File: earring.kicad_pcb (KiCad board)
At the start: 2 copper layers, 39.4 x 41.9 mm, 98 parts, among them J2 USB_C_Receptacle_USB2.0, Q1 NMOS 20V 0.75A 500mΩ@4.5V, Q2 NMOS 20V 0.75A 500mΩ@4.5V, Q3 NMOS 20V 0.75A 500mΩ@4.5V, Q4 NMOS 20V 0.75A 500mΩ@4.5V, U1 Magnetic Switch, U10 USBLC6-2P6, U20 LGS4056H, U3 RP2040, U4 W25Q16JV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

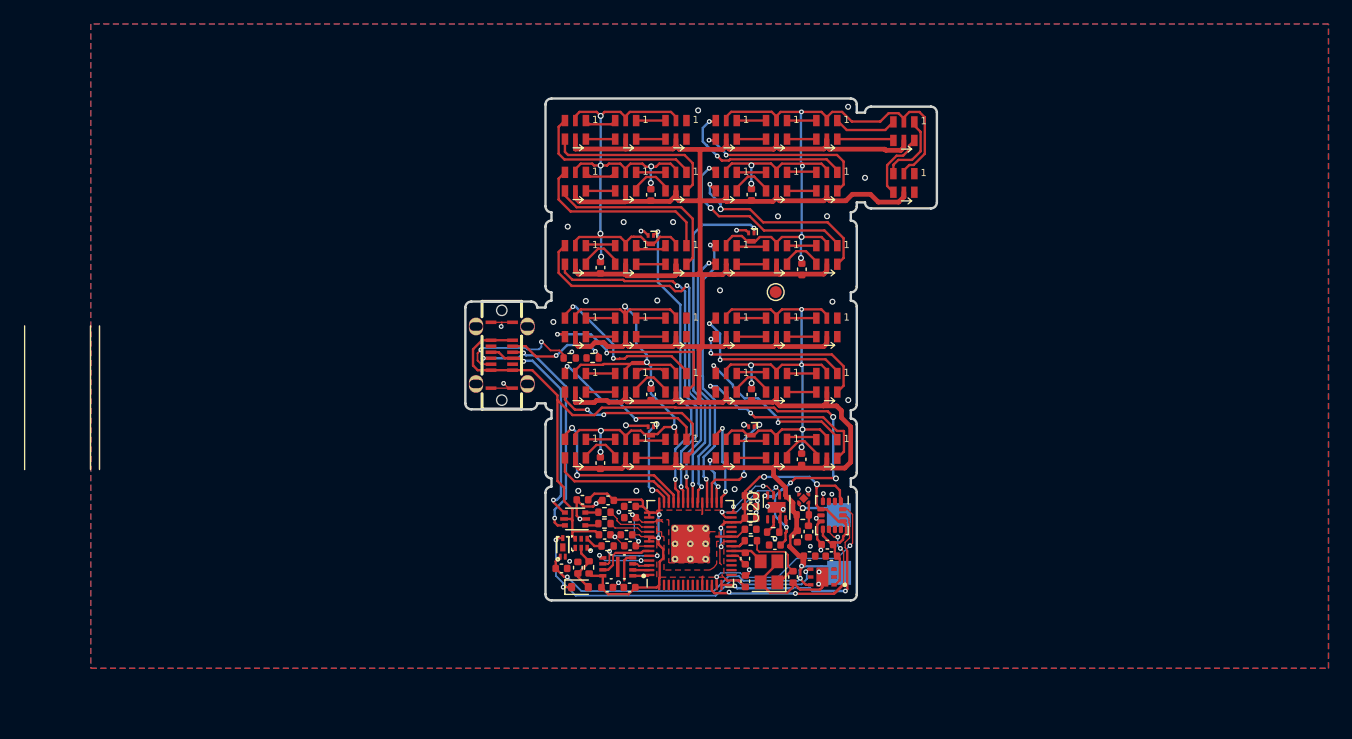
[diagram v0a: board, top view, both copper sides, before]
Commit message: Updated files, nearly complete. Added stiffener layer.
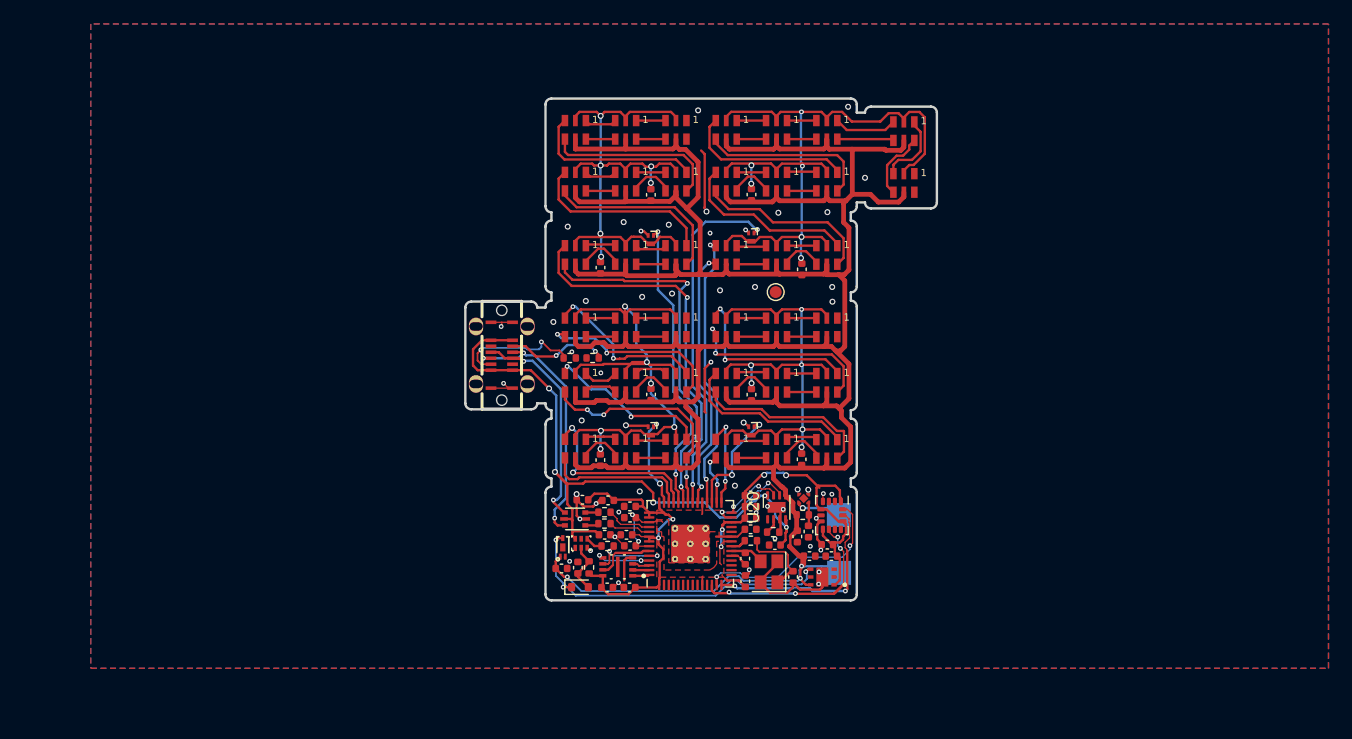
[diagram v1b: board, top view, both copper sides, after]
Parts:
- R10: value ~ -> 20k
- U9: value ~ -> NCP730BMT330TBG
- moved C26 0.25 mm to (154.6, 93.2)
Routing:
- net VBUS: track 71.2 -> 55.6 mm
- net +BATT: track 248.7 -> 264.0 mm
- net GND: track 38.2 -> 47.0 mm, vias 45 -> 51
- net +3V3: track 61.9 -> 64.0 mm
- net Net-(U34-CKL): track 16.9 -> 15.0 mm, vias 2 -> 0
- net Net-(U34-SDI): track 16.6 -> 14.9 mm, vias 2 -> 0
- net /LED_SCK_3: track 30.0 -> 31.1 mm
- net Net-(U27-CKL): track 15.3 -> 14.3 mm, vias 2 -> 0
- net Net-(U19-CKL): track 15.9 -> 14.9 mm, vias 2 -> 0
- net /LED_TX_4: track 14.7 -> 15.7 mm
- net Net-(U16-CKL): track 15.6 -> 16.5 mm
- net /LED_SCK_4: track 11.2 -> 12.1 mm
- net Net-(U27-SDI): track 15.0 -> 14.1 mm, vias 2 -> 0
- net /LED_TX_3: track 33.2 -> 32.4 mm
- net Net-(U15-CKO): track 16.5 -> 15.7 mm
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
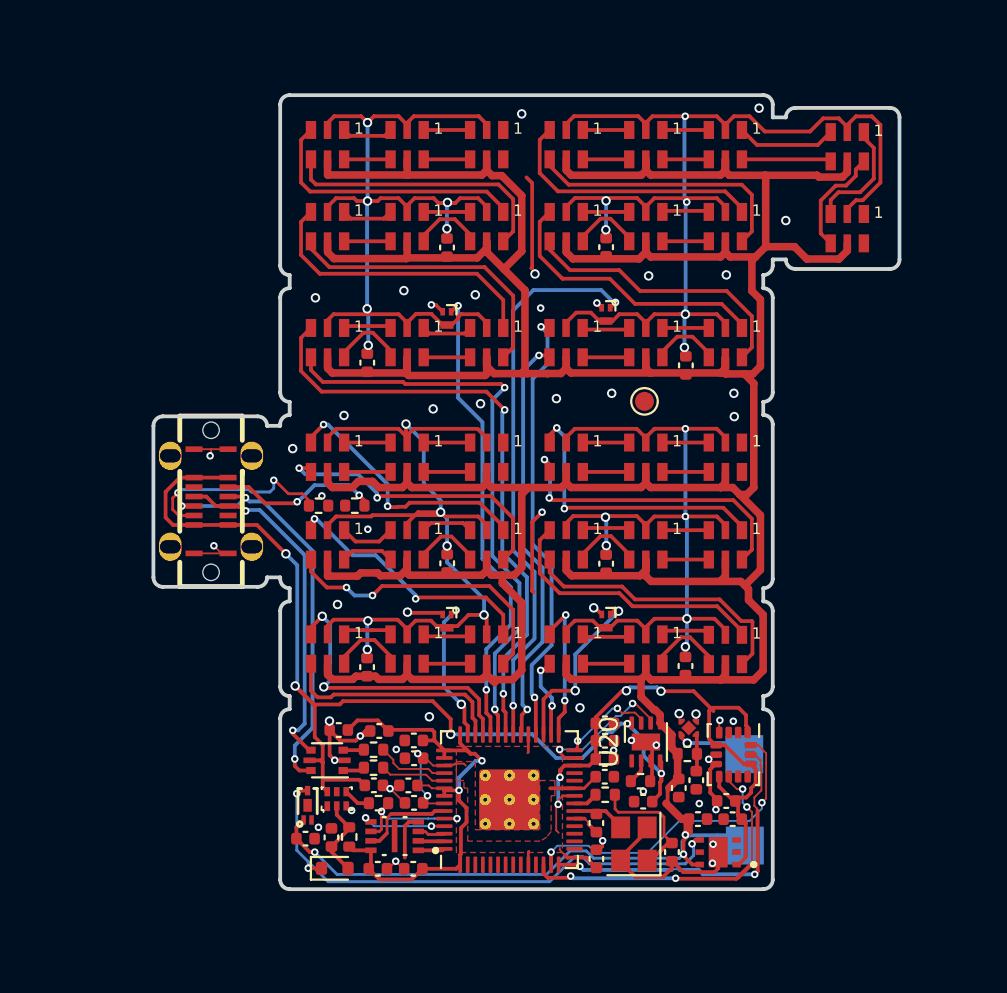
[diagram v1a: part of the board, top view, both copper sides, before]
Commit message: Add light sensor, add more 3d models.
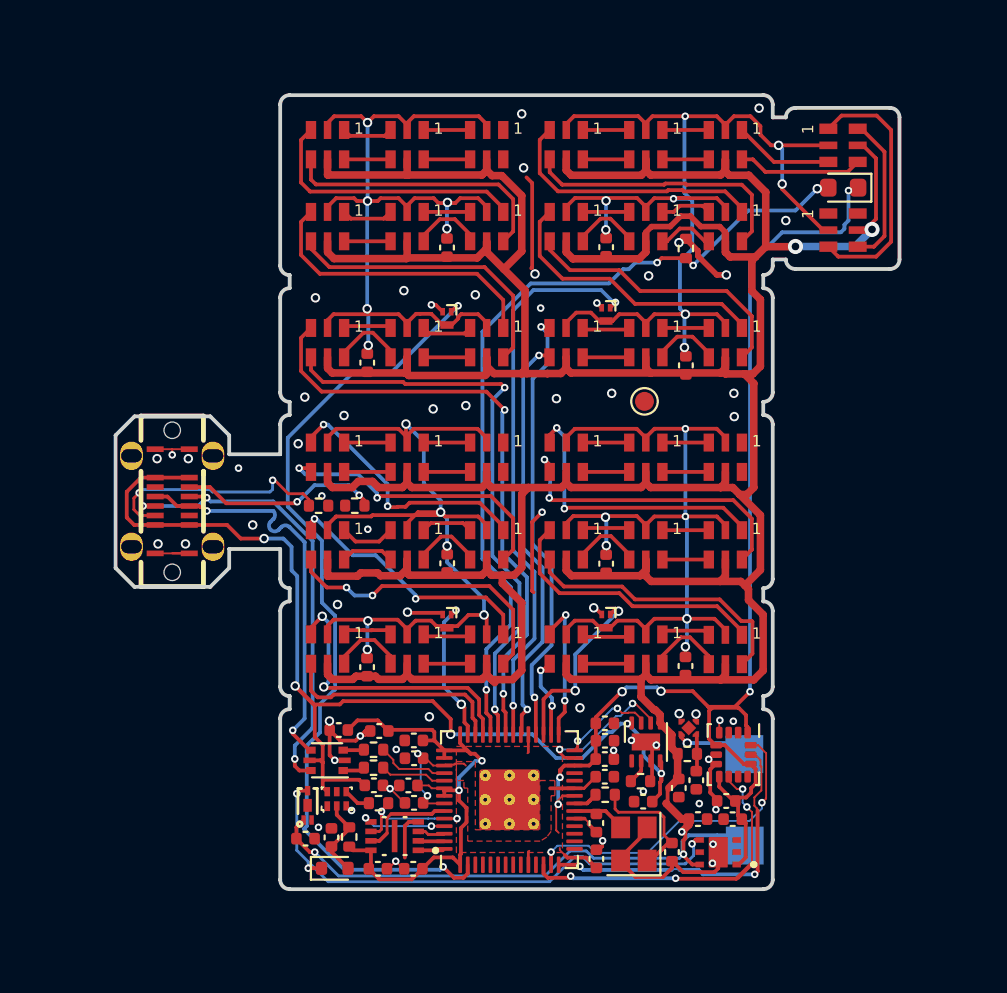
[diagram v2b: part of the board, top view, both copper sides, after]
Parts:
- added Q5: ~, LED_SMD:LED_0603_1608Metric, F.Cu at (179.7, 67.9)
- added R8: WHAT VALUE?, Resistor_SMD:R_0402_1005Metric, F.Cu at (171.4, 71.1)
- U24: value ~ -> SK9822-EC20
- moved J2 2.05 mm to (144.3, 84.5)
- moved U30 0.24 mm to (179.7, 65.7), turned to 90 degrees
- moved U37 0.24 mm to (179.7, 70.1), turned to 90 degrees
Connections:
- U3 pad 2: unconnected-(U3-GPIO0-Pad2) -> /SW_LED_3
- U3 pad 38: /SW_LED_3 -> /LIGHT_SENSE
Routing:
- net /LIGHT_SENSE: track 0.00 -> 44.2 mm, vias 0 -> 4
- net +3V3: track 64.0 -> 97.1 mm, vias 6 -> 8
- net /SW_LED_3: track 24.9 -> 45.1 mm
- net Net-(U30-SDO): track 6.16 -> 13.7 mm
- net /USB_D-: track 18.3 -> 21.6 mm
- net GND: track 47.0 -> 50.0 mm, vias 51 -> 59
- net VBUS: track 55.6 -> 58.1 mm
- net +BATT: track 264.0 -> 266.4 mm, vias 3 -> 5
- net /USB_D+: track 22.5 -> 24.9 mm
- net Net-(U30-CKO): track 5.80 -> 8.02 mm
- net Net-(J2-CC1): track 10.5 -> 12.6 mm
- net Net-(J2-CC2): track 8.55 -> 10.6 mm
- net Net-(U29-CKO): track 4.73 -> 6.60 mm
- net /LED_2_GND: track 61.5 -> 59.8 mm, vias 6 -> 8
- net Net-(U35-CKO): track 2.45 -> 3.01 mm
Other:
- board size 39.4 x 41.9 mm -> 41.4 x 41.9 mm

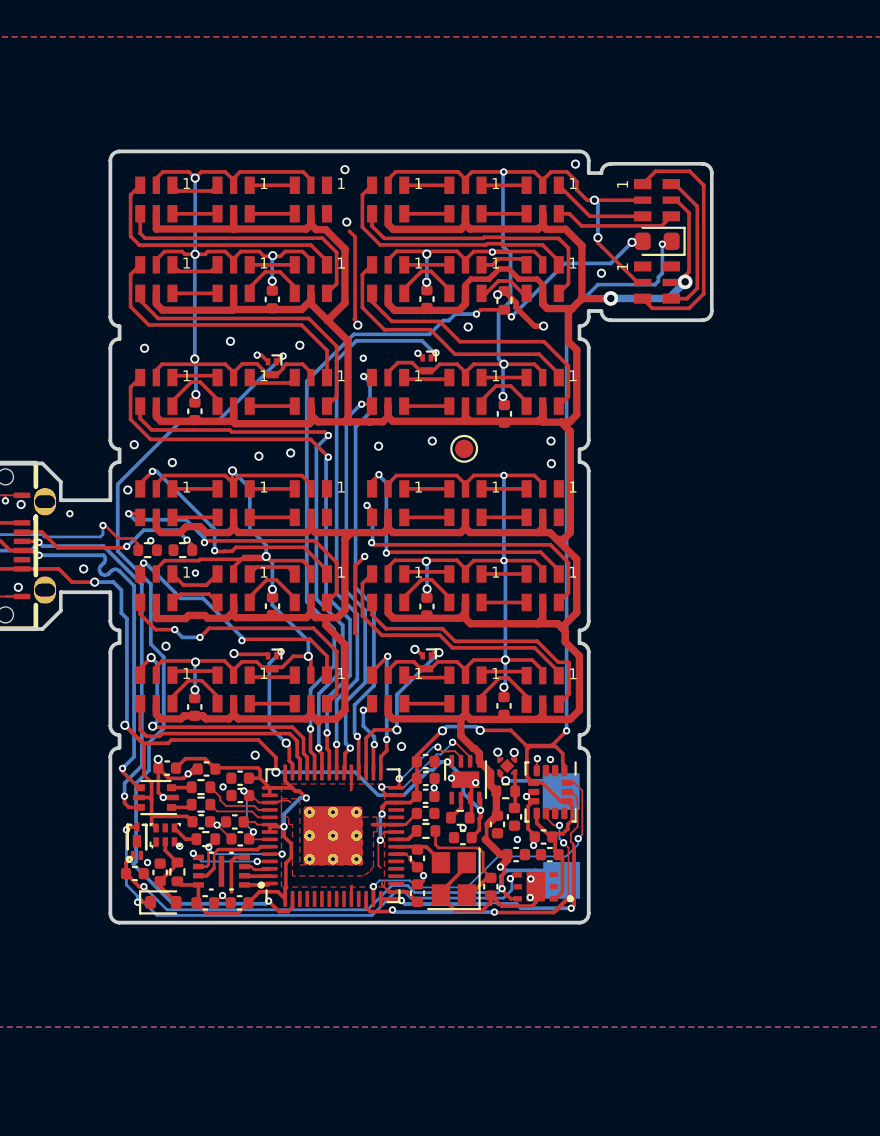
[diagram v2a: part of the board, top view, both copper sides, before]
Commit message: added silkscreen, debug contacts, and voltage monitoring
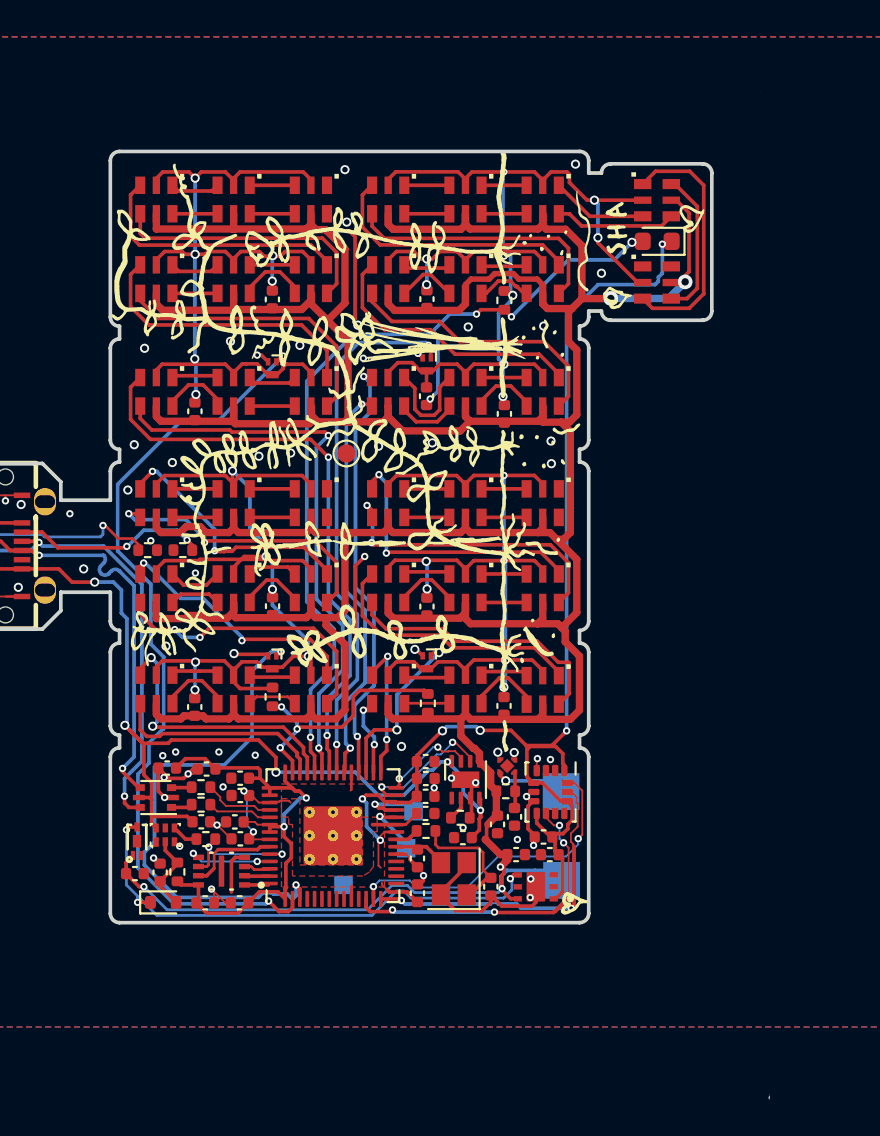
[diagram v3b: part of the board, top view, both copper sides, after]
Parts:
- added C33: 1u, Capacitor_SMD:C_0402_1005Metric, F.Cu at (167.2, 76.3)
- added G***: LOGO, LOGO, F.Cu at (161.5, 83.0)
- added R11: 40.2k, Resistor_SMD:R_0402_1005Metric, F.Cu at (167.3, 93.0)
- added R12: 100k, Resistor_SMD:R_0402_1005Metric, F.Cu at (158.8, 92.7)
- added TP4: TestPoint, TestPoint:TestPoint_Pad_1.0x1.0mm, B.Cu at (166.1, 100.9)
- added TP5: TestPoint, TestPoint:TestPoint_Pad_1.0x1.0mm, B.Cu at (166.5, 98.9)
- added TP6: TestPoint, TestPoint:TestPoint_Pad_1.0x1.0mm, B.Cu at (162.7, 102.9)
- Q5: value ~ -> light_sensor
- R8: value WHAT VALUE? -> 5.1k
- moved TP1 6.40 mm to (162.8, 79.4)
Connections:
- R8 pad 2: GND -> /LED_2_GND
- U3 pad 3: unconnected-(U3-GPIO1-Pad3) -> /SW_LED_4
- U3 pad 41: /SW_LED_4 -> /BATT_SENSE
- U9 pad 2: (no net) -> unconnected-(U9-NC/ADJ-Pad2)
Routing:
- net /SW_LED_4: track 7.66 -> 28.2 mm
- net /BATT_SENSE: track 0.00 -> 13.7 mm, vias 0 -> 3
- net /LIGHT_SENSE: track 44.2 -> 48.6 mm, vias 4 -> 5
- net SWD: track 0.00 -> 3.94 mm, vias 0 -> 1
- net SWCLK: track 0.00 -> 3.22 mm, vias 0 -> 1
- net Net-(U41-SDO): track 2.53 -> 5.54 mm
- net /LED_4_GND: track 47.6 -> 50.2 mm
- net GND: track 50.0 -> 47.9 mm, vias 59 -> 61
- net +3V3: track 97.1 -> 99.1 mm
- net Net-(U41-CKO): track 2.46 -> 3.40 mm
- net /LED_2_GND: vias 8 -> 9
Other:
- board text removed: "github.com/Twisted-Fields/ rp2040-motor-controller"
- board text removed: "pardon me, but ur board is upside down"

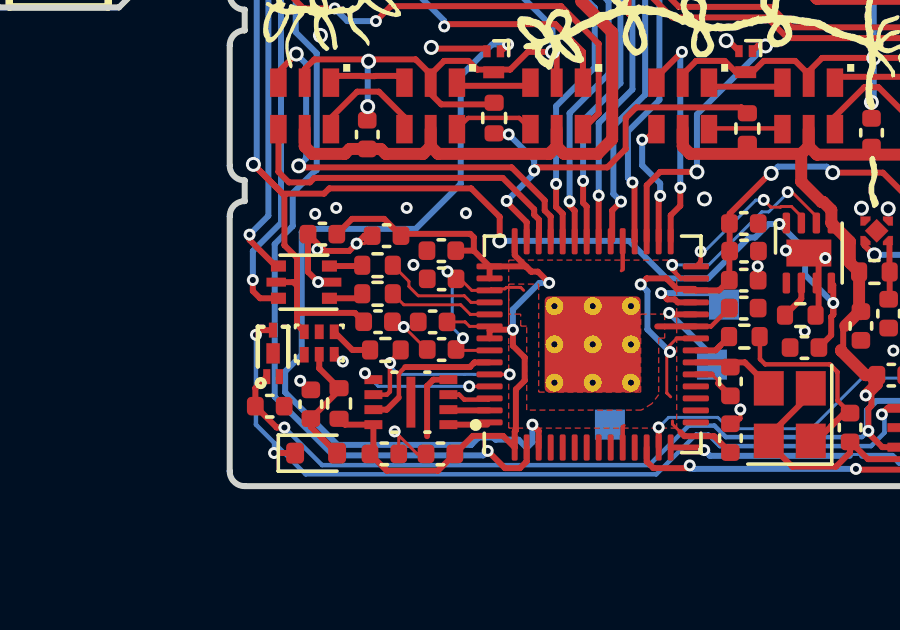
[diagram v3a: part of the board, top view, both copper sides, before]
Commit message: update stiffener layer
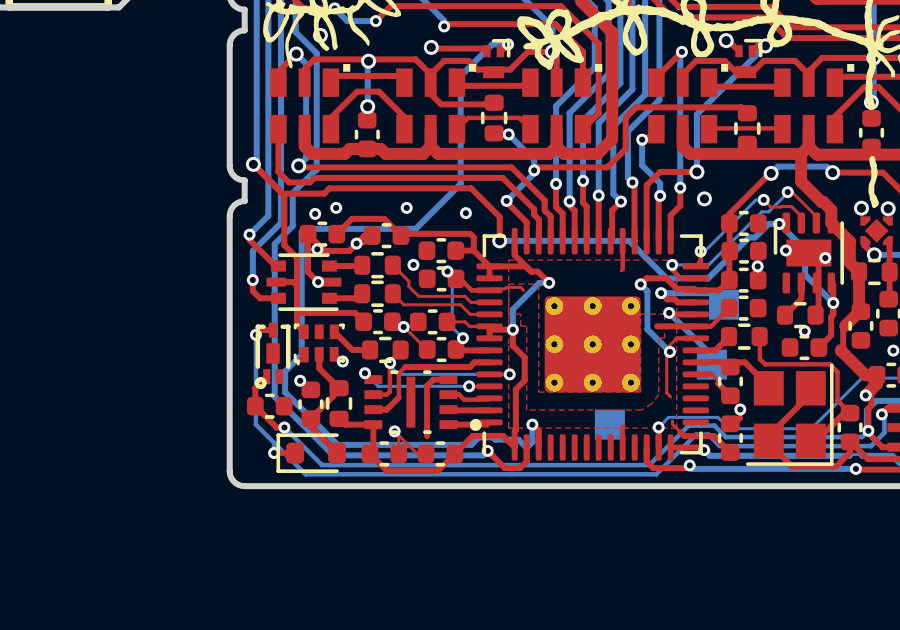
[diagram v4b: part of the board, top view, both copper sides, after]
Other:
- board text added: "GND"
- board text added: "SCK"
- board text added: "SWD"
